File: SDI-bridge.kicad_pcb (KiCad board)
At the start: 6 copper layers, 70 x 33 mm, 200 parts, among them J1 031-70526-21, J2 031-70526-21, J3 WE_68715014522_ONE-SIDE, J4 MC-HVT1-S04-G, J5 MC-HVT1-S04-G, J6 MC-HVT1-S04-G, U1 MAX8902B, U2 GS2971A, U3 GS2988, U4 CrossLink_LIF-MD6000-6JMG80I, U5 SC18IS602BIPW, Y1 ABM7_27.000MH_D2Y_T

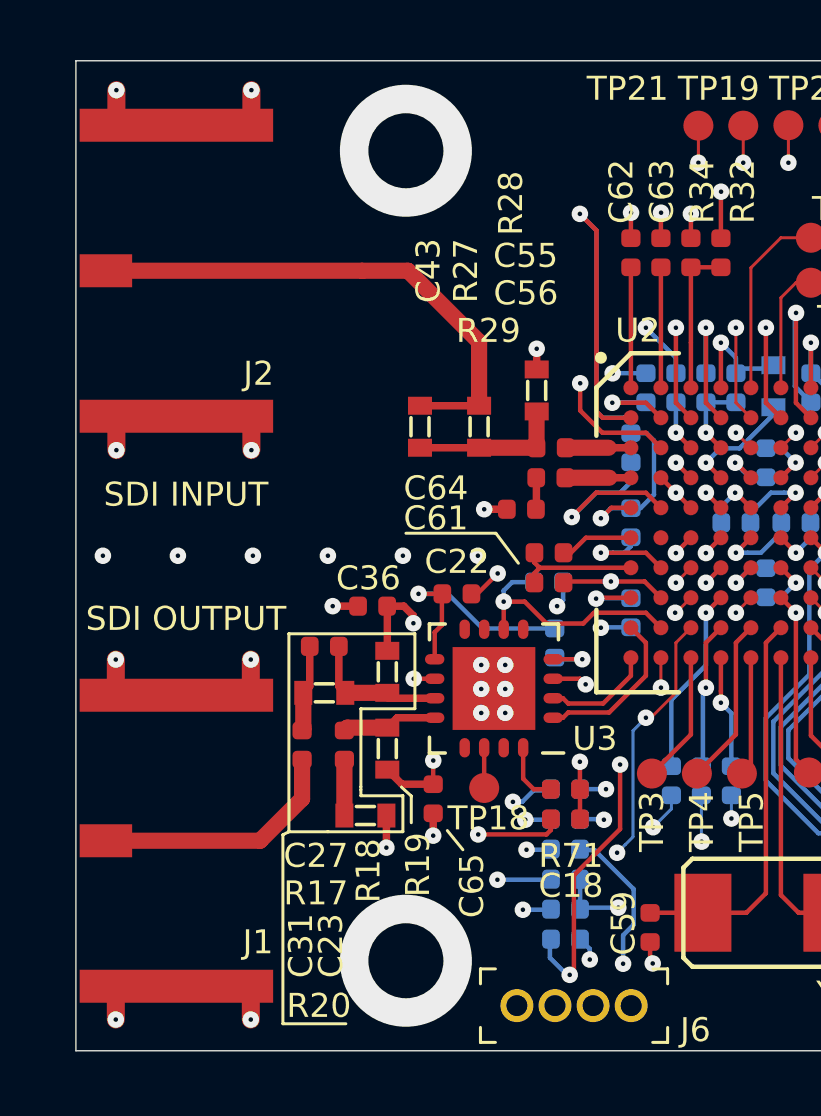
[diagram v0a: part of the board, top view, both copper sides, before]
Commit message: Switch In1.Cu with In4.Cu and add via fence
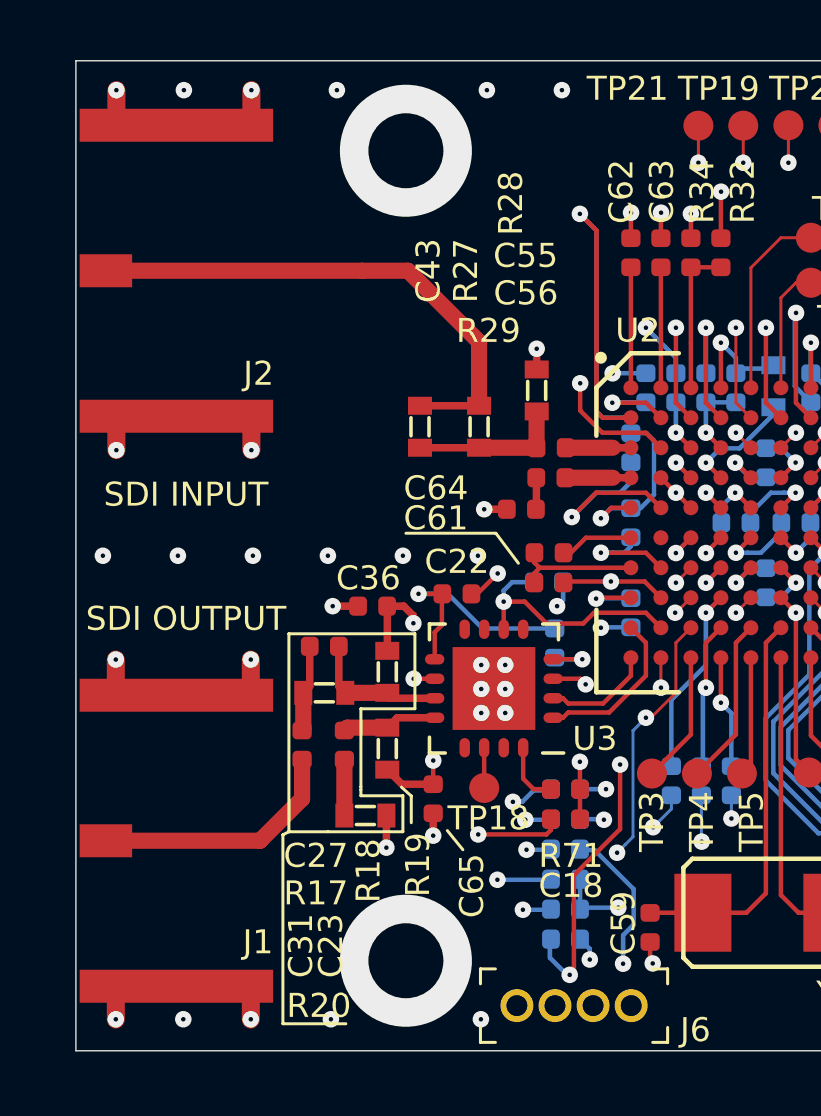
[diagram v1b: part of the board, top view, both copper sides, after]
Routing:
- net GNDA: vias 60 -> 67
- added copper zone on In4.Cu, net +1V2
- added copper zone on In4.Cu, net +3.3VA
- added copper zone on In4.Cu, net +3V3
- added copper zone on In1.Cu, net /GNDGPLL
- added copper zone on In1.Cu, net /GNDPLL_DPHY
- added copper zone on In2.Cu, net GNDA
- added copper zone on In1.Cu, net GNDREF
- added copper zone on In4.Cu, net IO_VDD
- added copper zone on In4.Cu, net VCCA_DPHY
- added copper zone on In4.Cu, net VCC_IO
- added copper zone on In4.Cu, net VPP
- removed copper zone on In1.Cu, net +1V2
- removed copper zone on In1.Cu, net +3.3VA
- removed copper zone on In1.Cu, net +3V3
- removed copper zone on In4.Cu, net /GNDGPLL
- removed copper zone on In4.Cu, net /GNDPLL_DPHY
- removed copper zone on In4.Cu, net GNDA
- removed copper zone on In2.Cu, net GNDREF
- removed copper zone on In4.Cu, net GNDREF
- removed copper zone on In1.Cu, net IO_VDD
- removed copper zone on In1.Cu, net VCCA_DPHY
- removed copper zone on In1.Cu, net VCC_IO
- removed copper zone on In1.Cu, net VPP
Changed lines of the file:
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@@
-(kicad_pcb (version 20171130) (host pcbnew 5.1.5)
+(kicad_pcb (version 20171130) (host pcbnew 5.1.5+dfsg1-2~bpo10+1)
   (general
     (thickness 1.6)
     (drawings 49)
-    (tracks 3888)
+    (tracks 3895)
     (zones 0)
     (modules 200)
@@
     (0 F.Cu signal)
     (1 In1.Cu power)
-    (2 In2.Cu power)
-    (3 In3.Cu signal)
-    (4 In4.Cu signal)
-    (31 B.Cu signal)
+    (2 In2.Cu power hide)
+    (3 In3.Cu signal hide)
+    (4 In4.Cu signal hide)
+    (31 B.Cu signal hide)
     (32 B.Adhes user hide)
     (33 F.Adhes user hide)
@@
   (gr_line (start 168 133) (end 98 133) (layer Edge.Cuts) (width 0.05))
   (via (at 111.4 116.5) (size 0.55) (drill 0.15) (layers F.Cu B.Cu) (net 0))
+  (via (at 106.5 131.95) (size 0.55) (drill 0.15) (layers F.Cu B.Cu) (net 3))
+  (via (at 111.5 131.95) (size 0.55) (drill 0.15) (layers F.Cu B.Cu) (net 3))
+  (via (at 101.58 131.95) (size 0.55) (drill 0.15) (layers F.Cu B.Cu) (net 3))
+  (via (at 114.2 100.98) (size 0.55) (drill 0.15) (layers F.Cu B.Cu) (net 3))
+  (via (at 106.7 100.98) (size 0.55) (drill 0.15) (layers F.Cu B.Cu) (net 3))
+  (via (at 111.7 100.98) (size 0.55) (drill 0.15) (layers F.Cu B.Cu) (net 3))
+  (via (at 101.6 100.98) (size 0.55) (drill 0.15) (layers F.Cu B.Cu) (net 3))
   (via (at 147.195 115.0775) (size 0.55) (drill 0.15) (layers F.Cu B.Cu) (net 1))
   (segment (start 147.0325 115.24) (end 147.195 115.0775) (width 0.1) (layer F.Cu) (net 1))
@@
   (segment (start 103.83 121.03) (end 103.83 119.96) (width 0.6) (layer F.Cu) (net 3))
   (segment (start 99.43 121.13) (end 99.33 121.03) (width 0.6) (layer F.Cu) (net 3))
-  (via (at 99.33 131.96) (size 0.55) (drill 0.15) (layers F.Cu B.Cu) (net 3))
-  (via (at 103.83 131.96) (size 0.55) (drill 0.15) (layers F.Cu B.Cu) (net 3))
+  (via (at 99.33 131.95) (size 0.55) (drill 0.15) (layers F.Cu B.Cu) (net 3))
+  (via (at 103.83 131.95) (size 0.55) (drill 0.15) (layers F.Cu B.Cu) (net 3))
   (segment (start 101.33 121.13) (end 103.73 121.13) (width 0.6) (layer F.Cu) (net 3))
   (segment (start 103.73 121.13) (end 103.83 121.03) (width 0.6) (layer F.Cu) (net 3))
@@
   (segment (start 140.44 116.08) (end 140.725 115.795) (width 0.1) (layer B.Cu) (net 189))
   (segment (start 114.305 112.9) (end 114.285 112.88) (width 0.15) (layer F.Cu) (net 190))
-  (segment (start 115.76 112.9) (end 114.305 112.9) (width 0.54) (layer F.Cu) (net 190))
-  (segment (start 116.5 112.9) (end 115.76 112.9) (width 0.25) (layer F.Cu) (net 190))
+  (segment (start 115.9 112.9) (end 114.305 112.9) (width 0.54) (layer F.Cu) (net 190))
+  (segment (start 116.5 112.9) (end 115.9 112.9) (width 0.25) (layer F.Cu) (net 190))
   (segment (start 125.98 107.15) (end 125.98 108.03) (width 0.1) (layer F.Cu) (net 191))
   (via (at 126.26 108.3) (size 0.55) (drill 0.15) (layers F.Cu B.Cu) (net 191))
@@
   (segment (start 140.63 108.94) (end 139.92 108.94) (width 0.1) (layer In2.Cu) (net 194))
   (segment (start 114.305 113.9) (end 114.285 113.88) (width 0.15) (layer F.Cu) (net 195))
-  (segment (start 115.78 113.9) (end 114.305 113.9) (width 0.54) (layer F.Cu) (net 195))
-  (segment (start 116.5 113.9) (end 115.78 113.9) (width 0.25) (layer F.Cu) (net 195))
+  (segment (start 115.9 113.9) (end 114.305 113.9) (width 0.54) (layer F.Cu) (net 195))
+  (segment (start 116.5 113.9) (end 115.9 113.9) (width 0.25) (layer F.Cu) (net 195))
   (segment (start 114.41 121.425) (end 115.575 121.425) (width 0.15) (layer F.Cu) (net 196))
   (segment (start 114.235 121.25) (end 114.41 121.425) (width 0.15) (layer F.Cu) (net 196))
@@
   (segment (start 114.235 121.9) (end 114.41 121.725) (width 0.15) (layer F.Cu) (net 197))
   (segment (start 113.91 121.9) (end 114.235 121.9) (width 0.15) (layer F.Cu) (net 197))
-  (zone (net 3) (net_name GNDA) (layer In4.Cu) (hatch edge 0.508)
+  (zone (net 3) (net_name GNDA) (layer In1.Cu) (hatch edge 0.508)
     (connect_pads (clearance 0.2))
     (min_thickness 0.254)
@@
     )
   )
-  (zone (net 79) (net_name /GNDGPLL) (layer In4.Cu) (hatch edge 0.508)
+  (zone (net 79) (net_name /GNDGPLL) (layer In1.Cu) (hatch edge 0.508)
     (connect_pads (clearance 0.2))
     (min_thickness 0.254)
@@
     )
   )
-  (zone (net 1) (net_name GNDREF) (layer In4.Cu) (hatch edge 0.508)
+  (zone (net 1) (net_name GNDREF) (layer In1.Cu) (hatch edge 0.508)
     (connect_pads (clearance 0.2))
     (min_thickness 0.254)
@@
     )
   )
-  (zone (net 78) (net_name /GNDPLL_DPHY) (layer In4.Cu) (hatch edge 0.508)
+  (zone (net 78) (net_name /GNDPLL_DPHY) (layer In1.Cu) (hatch edge 0.508)
     (connect_pads (clearance 0.2))
     (min_thickness 0.254)
@@
     )
   )
-  (zone (net 4) (net_name VPP) (layer In1.Cu) (hatch edge 0.508)
+  (zone (net 4) (net_name VPP) (layer In4.Cu) (hatch edge 0.508)
     (connect_pads (clearance 0.15))
     (min_thickness 0.15)
@@
     )
   )
-  (zone (net 2) (net_name +1V2) (layer In1.Cu) (hatch edge 0.508)
+  (zone (net 2) (net_name +1V2) (layer In4.Cu) (hatch edge 0.508)
     (connect_pads (clearance 0.15))
     (min_thickness 0.15)
@@
     )
   )
-  (zone (net 6) (net_name +3V3) (layer In1.Cu) (hatch edge 0.508)
+  (zone (net 6) (net_name +3V3) (layer In4.Cu) (hatch edge 0.508)
     (connect_pads (clearance 0.15))
     (min_thickness 0.15)
@@
     (polygon
       (pts
-        (xy 168 133) (xy 110.25 133) (xy 110.25 128) (xy 139.75 128) (xy 139.75 125.5)
+        (xy 168 133) (xy 98 133) (xy 98 128) (xy 139.75 128) (xy 139.75 125.5)
         (xy 143.25 125.5) (xy 143.25 130.5) (xy 153.25 130.5) (xy 153.25 109) (xy 149.5 109)
         (xy 149.5 100) (xy 168 100)
@@
     )
   )
-  (zone (net 5) (net_name +3.3VA) (layer In1.Cu) (hatch edge 0.508)
+  (zone (net 5) (net_name +3.3VA) (layer In4.Cu) (hatch edge 0.508)
     (connect_pads (clearance 0.15))
     (min_thickness 0.15)
@@
     (polygon
       (pts
-        (xy 120 106) (xy 111.75 106) (xy 111.75 125.5) (xy 139.5 125.5) (xy 139.5 127.75)
-        (xy 110.25 127.75) (xy 110.25 100) (xy 120 100)
+        (xy 120 106) (xy 109 106) (xy 109 125.5) (xy 139.5 125.5) (xy 139.5 127.75)
+        (xy 98 127.75) (xy 98 100) (xy 120 100)
       )
     )
   )
-  (zone (net 173) (net_name VCC_IO) (layer In1.Cu) (hatch edge 0.508)
+  (zone (net 173) (net_name VCC_IO) (layer In4.Cu) (hatch edge 0.508)
     (connect_pads (clearance 0.2))
     (min_thickness 0.254)
@@
     )
   )
-  (zone (net 170) (net_name IO_VDD) (layer In1.Cu) (hatch edge 0.508)
+  (zone (net 170) (net_name IO_VDD) (layer In4.Cu) (hatch edge 0.508)
     (connect_pads (clearance 0.15))
     (min_thickness 0.15)
@@
       (pts
         (xy 130.25 117.25) (xy 123.25 117.25) (xy 123.25 109.75) (xy 114.5 109.75) (xy 114.5 123)
-        (xy 147 123) (xy 147 125.25) (xy 112 125.25) (xy 112 106.25) (xy 120.25 106.25)
+        (xy 147 123) (xy 147 125.25) (xy 109.25 125.25) (xy 109.25 106.25) (xy 120.25 106.25)
         (xy 120.25 100) (xy 130.25 100)
       )
@@
     )
   )
-  (zone (net 5) (net_name +3.3VA) (layer In1.Cu) (hatch edge 0.508)
+  (zone (net 5) (net_name +3.3VA) (layer In4.Cu) (hatch edge 0.508)
     (connect_pads (clearance 0.15))
     (min_thickness 0.15)
@@
     )
   )
-  (zone (net 171) (net_name VCCA_DPHY) (layer In1.Cu) (hatch edge 0.508)
+  (zone (net 171) (net_name VCCA_DPHY) (layer In4.Cu) (hatch edge 0.508)
     (connect_pads (clearance 0.15))
     (min_thickness 0.15)
@@
     )
   )
-  (zone (net 1) (net_name GNDREF) (layer In2.Cu) (hatch edge 0.508)
+  (zone (net 3) (net_name GNDA) (layer In2.Cu) (hatch edge 0.508)
     (connect_pads (clearance 0.15))
     (min_thickness 0.15)
@@
     (polygon
       (pts
-        (xy 110.25 133) (xy 98 133) (xy 98 117.75) (xy 110.25 117.75)
+        (xy 110.25 131.5) (xy 98 131.5) (xy 98 117.75) (xy 110.25 117.75)
       )
     )
@@
     (polygon
       (pts
-        (xy 110.25 115.25) (xy 98 115.25) (xy 98 100) (xy 110.25 100)
+        (xy 116 102.75) (xy 116 112.5) (xy 117 112.5) (xy 117 114.25) (xy 116 114.25)
+        (xy 116 115.25) (xy 98 115.25) (xy 98 101.5) (xy 116 101.5)
       )
     )
@@
       )
     )
-  )
-  (zone (net 3) (net_name GNDA) (layer In1.Cu) (hatch edge 0.508)
-    (connect_pads (clearance 0.15))
-    (min_thickness 0.15)
-    (fill yes (arc_segments 32) (thermal_gap 0.508) (thermal_bridge_width 0.508))
-    (polygon
-      (pts
-        (xy 110 117.5) (xy 98 117.5) (xy 98 115.5) (xy 110 115.5)
-      )
-    )

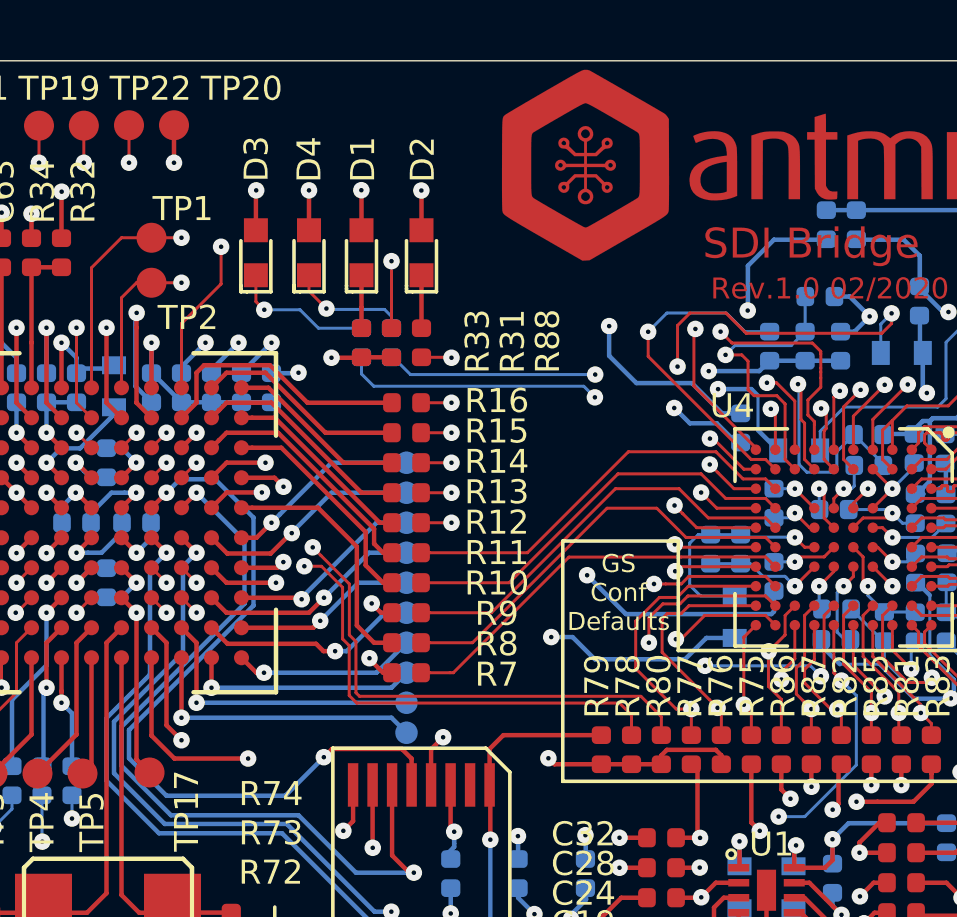
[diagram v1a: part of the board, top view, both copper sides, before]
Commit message: Tune parallel signal length
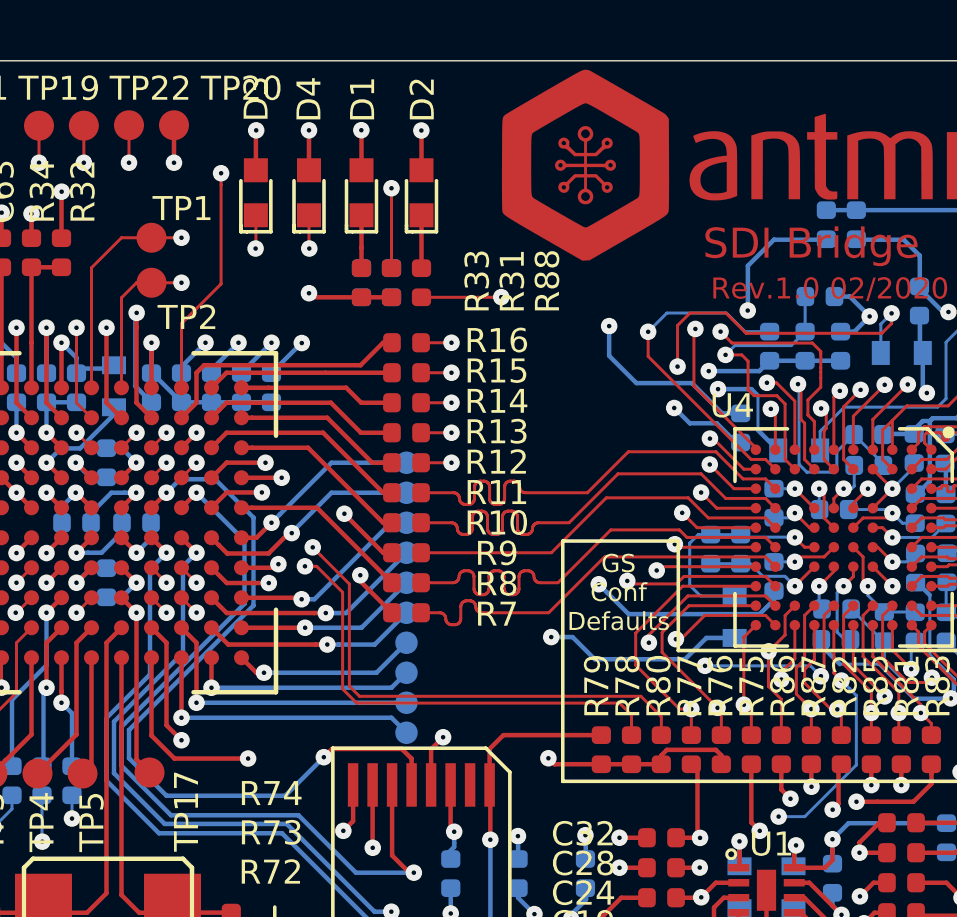
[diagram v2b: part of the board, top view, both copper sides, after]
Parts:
- moved D1 2.00 mm to (129.5, 104.4)
- moved D2 2.00 mm to (131.5, 104.4)
- moved D3 2.00 mm to (126.0, 104.4)
- moved D4 2.00 mm to (127.8, 104.4)
- moved R10 2.00 mm to (131.0, 115.4)
- moved R11 2.00 mm to (131.0, 114.4)
- moved R12 2.00 mm to (131.0, 113.4)
- moved R13 2.00 mm to (131.0, 112.4)
- moved R14 2.00 mm to (131.0, 111.4)
- moved R15 2.00 mm to (131.0, 110.4)
- moved R16 2.00 mm to (131.0, 109.4)
- moved R31 2.00 mm to (130.5, 107.4)
- moved R33 2.00 mm to (129.5, 107.4)
- moved R7 2.00 mm to (131.0, 118.4)
- moved R8 2.00 mm to (131.0, 117.4)
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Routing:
- net /LED_1: track 20.9 -> 11.4 mm, vias 2 -> 1
- net /LED_2: track 16.0 -> 7.84 mm, vias 2 -> 1
- net /DOUT17: track 12.1 -> 16.8 mm
- net Net-(D3-Pad1): track 4.77 -> 1.11 mm
- net /DOUT18: track 12.2 -> 15.8 mm
- net /PCLK: track 32.4 -> 35.8 mm
- net /D10: track 11.3 -> 8.00 mm
- net Net-(D4-Pad1): track 4.02 -> 1.11 mm
- net /D12: track 11.8 -> 8.88 mm
- net /D11: track 8.42 -> 6.05 mm
- net /DOUT15: track 14.0 -> 16.3 mm
- net /DOUT16: track 13.1 -> 15.3 mm
- net /DOUT13: track 13.8 -> 15.8 mm
- net /V_VSYNC: track 32.0 -> 33.8 mm
- net /DOUT11: track 14.2 -> 15.7 mm
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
